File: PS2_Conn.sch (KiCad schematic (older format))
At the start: 3 parts

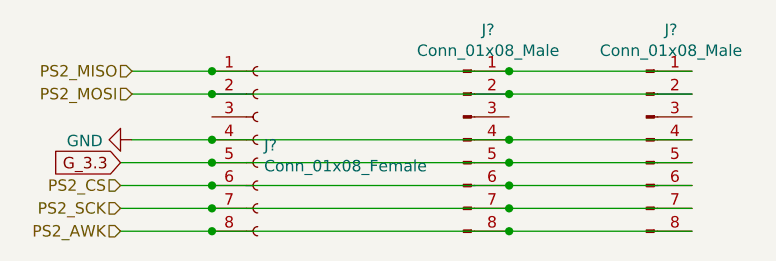
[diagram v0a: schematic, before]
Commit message: added the needed footprints
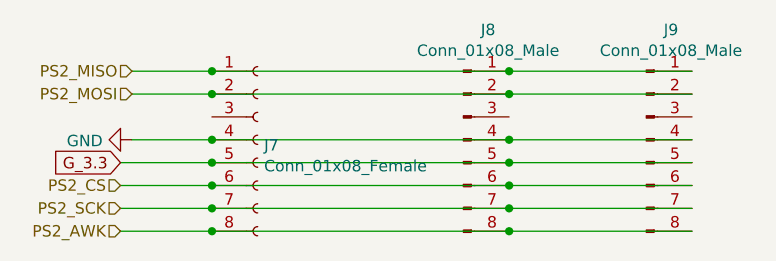
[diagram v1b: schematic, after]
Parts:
- J7, J8, J9: renamed from J?; footprint (none) -> Connector_PinHeader_2.54mm:PinHeader_1x08_P2.54mm_Vertical
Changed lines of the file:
@@
 PS2_MOSI
 $Comp
-L Connector:Conn_01x08_Male J?
+L Connector:Conn_01x08_Male J9
 U 1 1 5FD08425
 P 6350 3200
-F 0 "J?" H 6458 3681 50  0000 C CNN
+F 0 "J9" H 6458 3681 50  0000 C CNN
 F 1 "Conn_01x08_Male" H 6458 3590 50  0000 C CNN
-F 2 "" H 6350 3200 50  0001 C CNN
+F 2 "Connector_PinHeader_2.54mm:PinHeader_1x08_P2.54mm_Vertical" H 6350 3200 50  0001 C CNN
 F 3 "~" H 6350 3200 50  0001 C CNN
 	1    6350 3200
@@
 $EndComp
 $Comp
-L Connector:Conn_01x08_Male J?
+L Connector:Conn_01x08_Male J8
 U 1 1 5FD09C2F
 P 5550 3200
-F 0 "J?" H 5658 3681 50  0000 C CNN
+F 0 "J8" H 5658 3681 50  0000 C CNN
 F 1 "Conn_01x08_Male" H 5658 3590 50  0000 C CNN
-F 2 "" H 5550 3200 50  0001 C CNN
+F 2 "Connector_PinHeader_2.54mm:PinHeader_1x08_P2.54mm_Vertical" H 5550 3200 50  0001 C CNN
 F 3 "~" H 5550 3200 50  0001 C CNN
 	1    5550 3200
@@
 $EndComp
 $Comp
-L Connector:Conn_01x08_Female J?
+L Connector:Conn_01x08_Female J7
 U 1 1 5FD0A29B
 P 4650 3200
-F 0 "J?" H 4678 3176 50  0000 L CNN
+F 0 "J7" H 4678 3176 50  0000 L CNN
 F 1 "Conn_01x08_Female" H 4678 3085 50  0000 L CNN
-F 2 "" H 4650 3200 50  0001 C CNN
+F 2 "Connector_PinHeader_2.54mm:PinHeader_1x08_P2.54mm_Vertical" H 4650 3200 50  0001 C CNN
 F 3 "~" H 4650 3200 50  0001 C CNN
 	1    4650 3200
@@
 $EndComp
 $Comp
-L power:GND #PWR?
+L power:GND #PWR021
 U 1 1 5FD0EB01
 P 4100 3200
-F 0 "#PWR?" H 4100 2950 50  0001 C CNN
+F 0 "#PWR021" H 4100 2950 50  0001 C CNN
 F 1 "GND" V 4105 3072 50  0000 R CNN
 F 2 "" H 4100 3200 50  0001 C CNN
